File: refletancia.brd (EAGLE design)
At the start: 82.3 x 68.3 mm, 27 parts

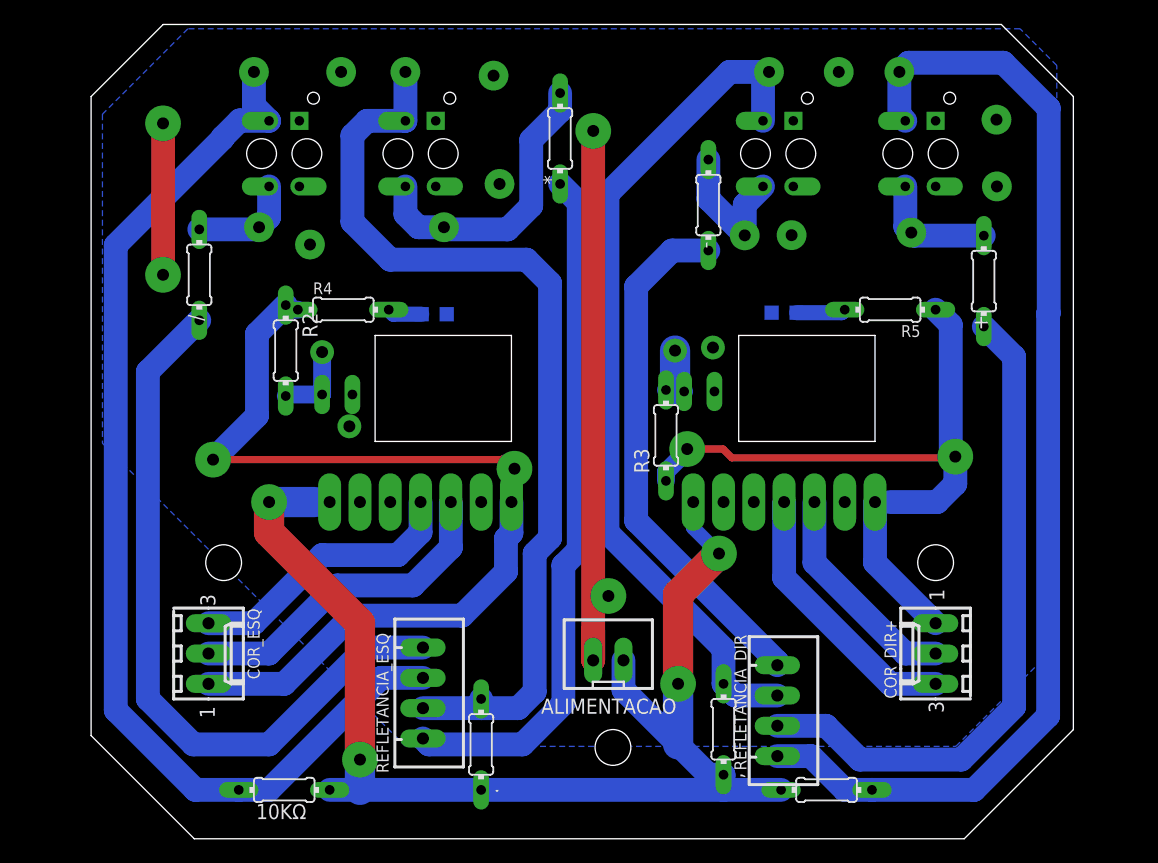
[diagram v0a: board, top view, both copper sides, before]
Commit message: Alteração da dimensão e posição de furos
Os furos de fixação foram alterados, a posição dos conectores do sensor de cor também foi alterada, a dimensão da placa também foi alterada assim como posição de várias trilhas foi trocada
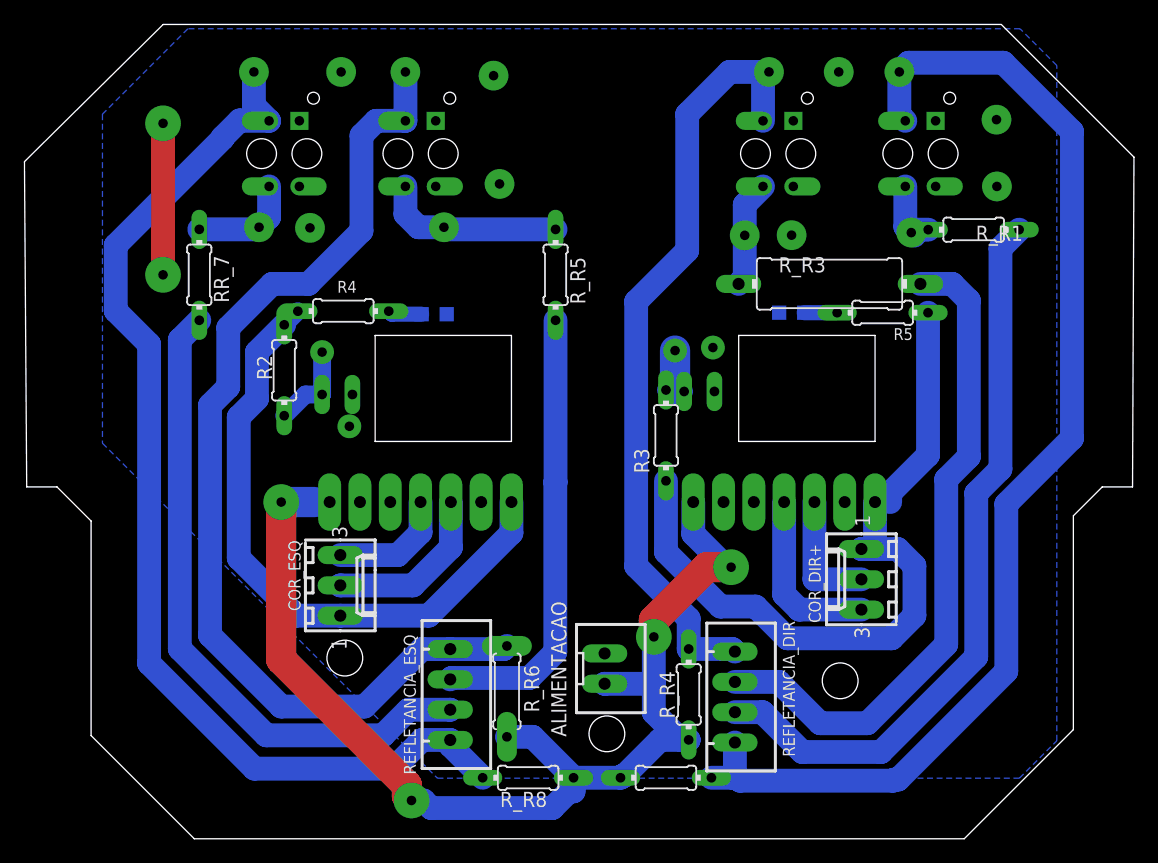
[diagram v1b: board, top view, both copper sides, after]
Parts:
- removed *, +, -: 260Ω, rcl_robotica:0204/7
- removed ,, ., R1: 10KΩ, rcl_robotica:0204/7
- removed 10KΩ: (no value), rcl_robotica:0204/7
- added R_R1, R_R5: 260Ω, rcl_robotica:0204/7
- added R_R2, R_R4, R_R8: 10KΩ, rcl_robotica:0204/7
- added R_R3: 260Ω, rcl_vitoria:0414/15_LOG_PAD
- added R_R6: 10KΩ, rcl_vitoria:0207/7_LONG_PAD2
- +DIR, +ESQ, DIR, ESQ: value TCRT5000 -> (none)
- COR_DIR+: value (none) -> 22-27-2031-03
- moved COR_ESQ 12.4 mm to (23.7, 41.3)
- moved COR_DIR+ 8.80 mm to (67.4, 41.8)
- moved REFLETANCIA_DIR 3.74 mm to (56.8, 31.9)
- moved REFLETANCIA_ESQ 2.29 mm to (33.0, 32.1)
- moved R2 1.66 mm to (19.1, 59.3)
- moved ALIMENTACAO 0.76 mm to (45.9, 34.3), turned to 270 degrees
- moved R5 0.68 mm to (69.2, 64.1)
- moved LED4 0.63 mm to (61.6, 64.1)
- moved R4 0.13 mm to (24.0, 64.3)
- renumbered +D to +ESQ, +E to +DIR, / to RR_7, D to ESQ, E to DIR
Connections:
- net +5V: now also R_R2.2, R_R4.2, R_R6.2, R_R8.2; no longer ,.2, ..2, 10KΩ.2, R1.2
- net ANALOG_+DIR.: now also R_R2.1; no longer R1.1
- net ANALOG_+ESQ: now also REFLETANCIA_ESQ.4, R_R8.1; no longer 10KΩ.1, REFLETANCIA_ESQ.2
- net ANALOG_DIR: now also REFLETANCIA_DIR.1, R_R4.1; no longer ,.1, REFLETANCIA_DIR.2
- net ANALOG_ESQ: now also REFLETANCIA_ESQ.1, R_R6.1; no longer ..1, REFLETANCIA_ESQ.3
- net DIGITAL_+DIR.: now also R_R1.1; no longer +.1
- net DIGITAL_+ESQ: now also REFLETANCIA_ESQ.3; no longer REFLETANCIA_ESQ.1
- net DIGITAL_DIR: now also REFLETANCIA_DIR.2, R_R3.1; no longer -.1, REFLETANCIA_DIR.1
- net DIGITAL_ESQ: now also REFLETANCIA_ESQ.2, R_R5.1; no longer *.1, REFLETANCIA_ESQ.4
- net N$1: now also R_R1.2; no longer +.2
- net N$2: now also R_R3.2; no longer -.2
- net N$3: now also R_R5.2; no longer *.2
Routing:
- net GND: track 59.6 -> 12.7 mm, vias 14 -> 12
- net N$7: track 80.1 -> 53.1 mm, vias 2 -> 0
- net DIGITAL_ESQ: track 58.1 -> 37.6 mm
- net N$9: track 23.5 -> 10.1 mm
- net N$8: track 27.8 -> 14.4 mm
- net DIGITAL_DIR: track 44.0 -> 56.1 mm
- net +5V: track 107.9 -> 98.2 mm
- net N$3: track 24.7 -> 15.4 mm
- net N$11: track 22.7 -> 14.8 mm
- net N$12: track 18.4 -> 10.4 mm
- net ANALOG_DIR: track 72.1 -> 65.0 mm
- net DIGITAL_+ESQ: track 61.5 -> 54.8 mm
- net DIGITAL_+DIR.: track 55.8 -> 62.2 mm
- net ANALOG_ESQ: track 80.5 -> 86.7 mm
- net ANALOG_+DIR.: track 96.1 -> 100.6 mm
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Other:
- board size 82.3 x 68.3 mm -> 93 x 68.3 mm
